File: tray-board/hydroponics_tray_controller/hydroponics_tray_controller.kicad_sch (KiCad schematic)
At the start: 29 parts, among them J1 Jumper, J2 Display_Connector, J4 Power_Comms, J5 i2c_Peripherals, J6 1Wire_Peripherals, SW1 RotaryEncoder_Switch, U1 ESP32, U2 SP3485EN, U3 AMS1117-3.3

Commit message: tray-board: replace ST7789 display connector with ILI9341 touch + SD card
J2 is now a 14-pin header matching the actual ILI9341/XPT2046 touch
display (VCC, GND, CS, RESET, DC, MOSI, SCK, LED, MISO, T_CLK, T_CS,
T_DIN, T_DO, T_IRQ), replacing the old 8-pin no-touch ST7789 wiring.
Added J3, a separate 4-pin SD card connector sharing the display SPI
bus with its own CS line. New signals use previously-unused ESP32
GPIOs 14, 19, 34, 35. Verified via KiCad 10 ERC and netlist export.

PCB footprints synced from the updated schematic (Update PCB from
Schematic) - placement and routing for the new pins still needed.

README updated with the corrected display spec and pin list.

Co-Authored-By: Claude Sonnet 5 <noreply@anthropic.com>
Claude-Session: https://claude.ai/code/session_01QYbZEgBzGJ6rSai1ie8nG1
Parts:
- added J3: SD_Connector, Connector_PinHeader_2.54mm:PinHeader_1x04_P2.54mm_Vertical, symbol Connector:Conn_01x04_Socket
- J2: value Display_Connector -> Display_Connector_Touch; footprint Connector_PinHeader_2.54mm:PinHeader_1x08_P2.54mm_Vertical -> Connector_PinHeader_2.54mm:PinHeader_1x14_P2.54mm_Vertical; symbol Connector:Conn_01x08_Socket -> Connector:Conn_01x14_Socket
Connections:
- net +3V3: now also J2.1 (Pin_1); no longer J2.2 (Pin_2)
- net ESP32_D18: now also J2.10 (Pin_10), J2.7 (Pin_7), J3.4 (Pin_4); no longer J2.3 (Pin_3)
- net ESP32_D2: now also J2.5 (Pin_5); no longer J2.6 (Pin_6)
- net ESP32_D23: now also J2.12 (Pin_12), J2.6 (Pin_6), J3.2 (Pin_2); no longer J2.4 (Pin_4)
- net ESP32_D4: now also J2.4 (Pin_4); no longer J2.5 (Pin_5)
- net ESP32_D5: now also J2.3 (Pin_3); no longer J2.7 (Pin_7)
- net GND: now also J2.2 (Pin_2); no longer J2.1 (Pin_1)
- net ESP32_D14: now reaches U1.10 (D14)
- net ESP32_D14: now also J2.11 (Pin_11)
- net ESP32_D19: now reaches U1.19 (D19)
- net ESP32_D19: now also J3.1 (Pin_1)
- net ESP32_D35: now reaches U1.22 (D35)
- net ESP32_D35: now also J2.14 (Pin_14)
- net ESP32_D34: now reaches U1.24 (D34)
- net ESP32_D34: now also J2.13 (Pin_13), J2.9 (Pin_9), J3.3 (Pin_3)
- no-connect marks 11 -> 7
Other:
- note added: "SD Card Connector"

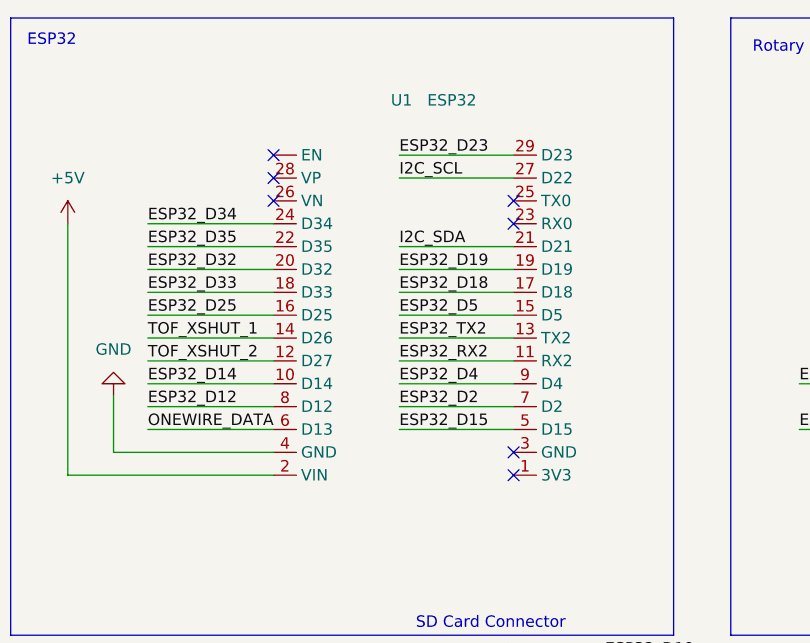
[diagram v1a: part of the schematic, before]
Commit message: JLCPCB prep: fab.sh cleanup, DNP the ESP32 module, BOM part-value fixes
tools/fab.sh:
- Gerbers use Protel extensions (JLCPCB's preferred naming) instead of
  --no-protel-ext.
- Drill export splits PTH/NPTH into separate Excellon files
  (--excellon-separate-th) instead of one merged file.
- BOM export now pulls the LCSC field (matching what's actually used in
  the schematics) instead of a nonexistent MPN field, groups by
  Value+Footprint+LCSC so parts sharing a value but not an LCSC code
  don't get merged together and silently lose their code, and excludes
  DNP parts.
- Pick-and-place (now named *-cpl.csv) already excluded DNP/THT; BOM
  now matches.
- Final zip only includes the gerbers + drill files JLCPCB needs, not
  the .gbrjob/drill-map files kicad-cli also generates.
- ERC gate relaxed to error-only: a stale lib_symbol_mismatch warning
  on the ESP32 symbol (harmless - doesn't affect connectivity or fab
  output) was blocking the pipeline; DRC stays error+warning.

Mark the socketed ESP32 DevKit (U1) Do-Not-Populate in both boards'
schematics, since it's a module the user fits themselves rather than
something JLCPCB should source/place - this drops it from BOM and CPL
automatically.

Fix a stale pin-number mismatch in reservoir-board's New_Library.kicad_sym
(ESP32 EN pin was "" in the library file but "30" in the schematic's
cached copy) that was one cause of the ERC warning above.

Also includes reservoir-board BOM part-value corrections (D_Schottky ->
SS34, bare resistor values -> "<value> Ohm") made directly in KiCad.

Co-Authored-By: Claude Sonnet 5 <noreply@anthropic.com>
Claude-Session: https://claude.ai/code/session_01QYbZEgBzGJ6rSai1ie8nG1
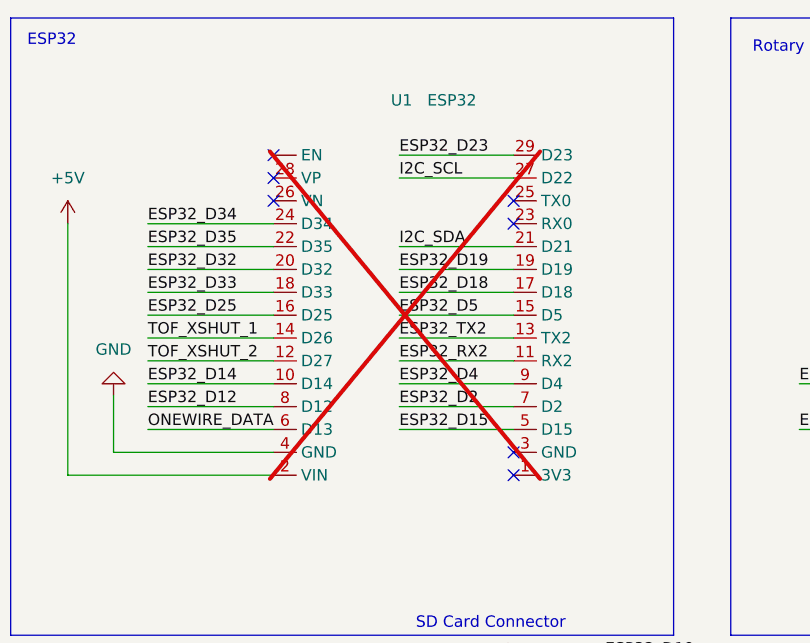
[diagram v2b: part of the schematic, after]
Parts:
- U1: now not fitted
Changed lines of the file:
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@@
 		(on_board yes)
 		(in_pos_files yes)
-		(dnp no)
+		(dnp yes)
 		(property "Reference" "U1"
 			(at 165.354 28.194 0)

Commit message: tray-board: fix EN pin number drift and J3 pin4 dangling wire
Same New_Library.kicad_sym drift as reservoir-board (EN pin number ""
in the library file vs "30" in the schematic's cached copy, matching
the ESP32_DevKit_30Pin footprint's pad "30") - tray-board's copy had
the same stale "" left over, just never triggered ERC since nothing
here referenced pin 30 by name at the time it was last checked.

J3 (SD connector) pin 4's wire started 1.27mm short of the actual pin
position - a leftover construction slip from when J3 was first added,
surfaced now as a real ERC error after the pin got moved during the
in-progress redesign. Fixed to reach the pin.

Co-Authored-By: Claude Sonnet 5 <noreply@anthropic.com>
Claude-Session: https://claude.ai/code/session_01QYbZEgBzGJ6rSai1ie8nG1
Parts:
- removed C6, C7: 100nF, Capacitor_SMD:C_0805_2012Metric, symbol Device:C
- removed R6, R7, R8: 10k, Resistor_SMD:R_0805_2012Metric, symbol Device:R
- removed SW1: RotaryEncoder_Switch, Rotary_Encoder:RotaryEncoder_Alps_EC11E-Switch_Vertical_H20mm, symbol Device:RotaryEncoder_Switch
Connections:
- net RS485_A: now also J4.3 (Pin_3); no longer J4.2 (Pin_2)
- net RS485_B: now also J4.2 (Pin_2); no longer J4.3 (Pin_3)
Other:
- note removed: "Rotary Encoder"
- moved on the sheet: J3

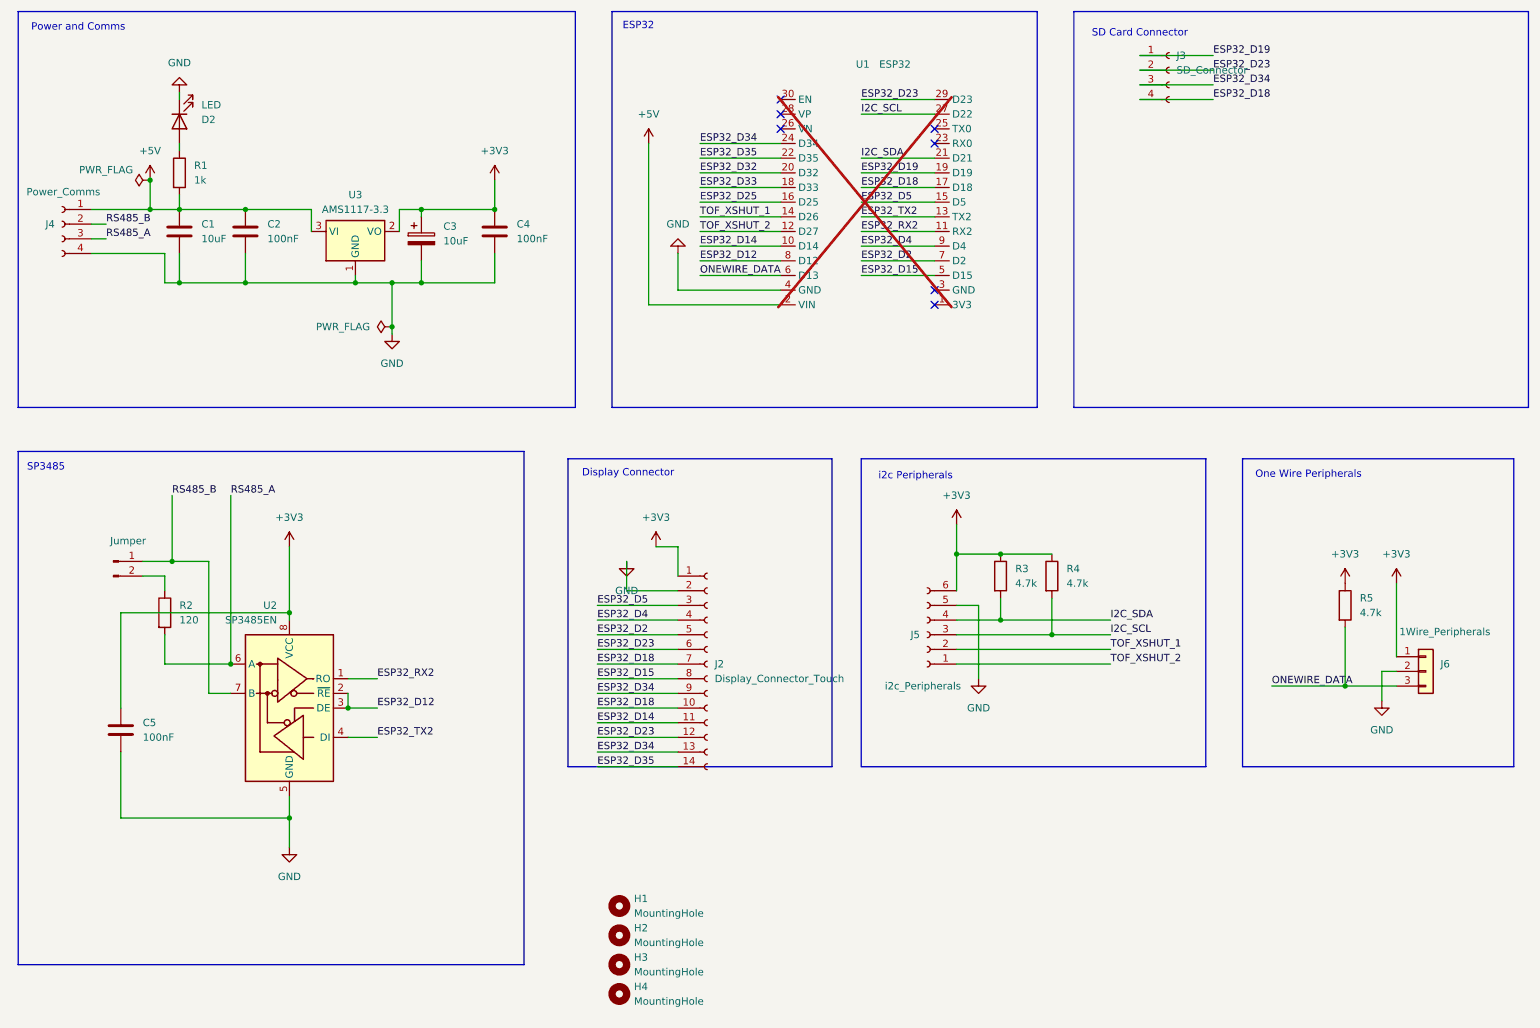
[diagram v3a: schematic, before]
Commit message: tray-board: merge display+SD connector into one symbol, fix SD pad position, re-sync PCB
- New_Library: merged the 14-pin main header and 4-pin SD header into a
  single Display_MSP2401_2.4in_Touch schematic symbol, matching the combined
  footprint's fixed connector spacing. J3 (standalone SD connector) removed;
  its nets are now carried by the merged symbol's SD1-SD4 pins.
- Footprint: fixed SD1-SD4 pad Y-coordinate (6.51mm -> 3.00mm from the top
  edge) - they sit in the same row as the two top mounting holes, per the
  mechanical drawing.
- Fixed H1-H4 mounting hole footprint (MountingHole_3.2mm_M3_Pad_Via ->
  MountingHole_3.2mm_M3) to match their "no connection" schematic symbol.
- kicad_pcb re-synced from schematic (Update PCB from Schematic + footprint
  reload) - layout/routing still in progress.

Co-Authored-By: Claude Sonnet 5 <noreply@anthropic.com>
Claude-Session: https://claude.ai/code/session_01QYbZEgBzGJ6rSai1ie8nG1
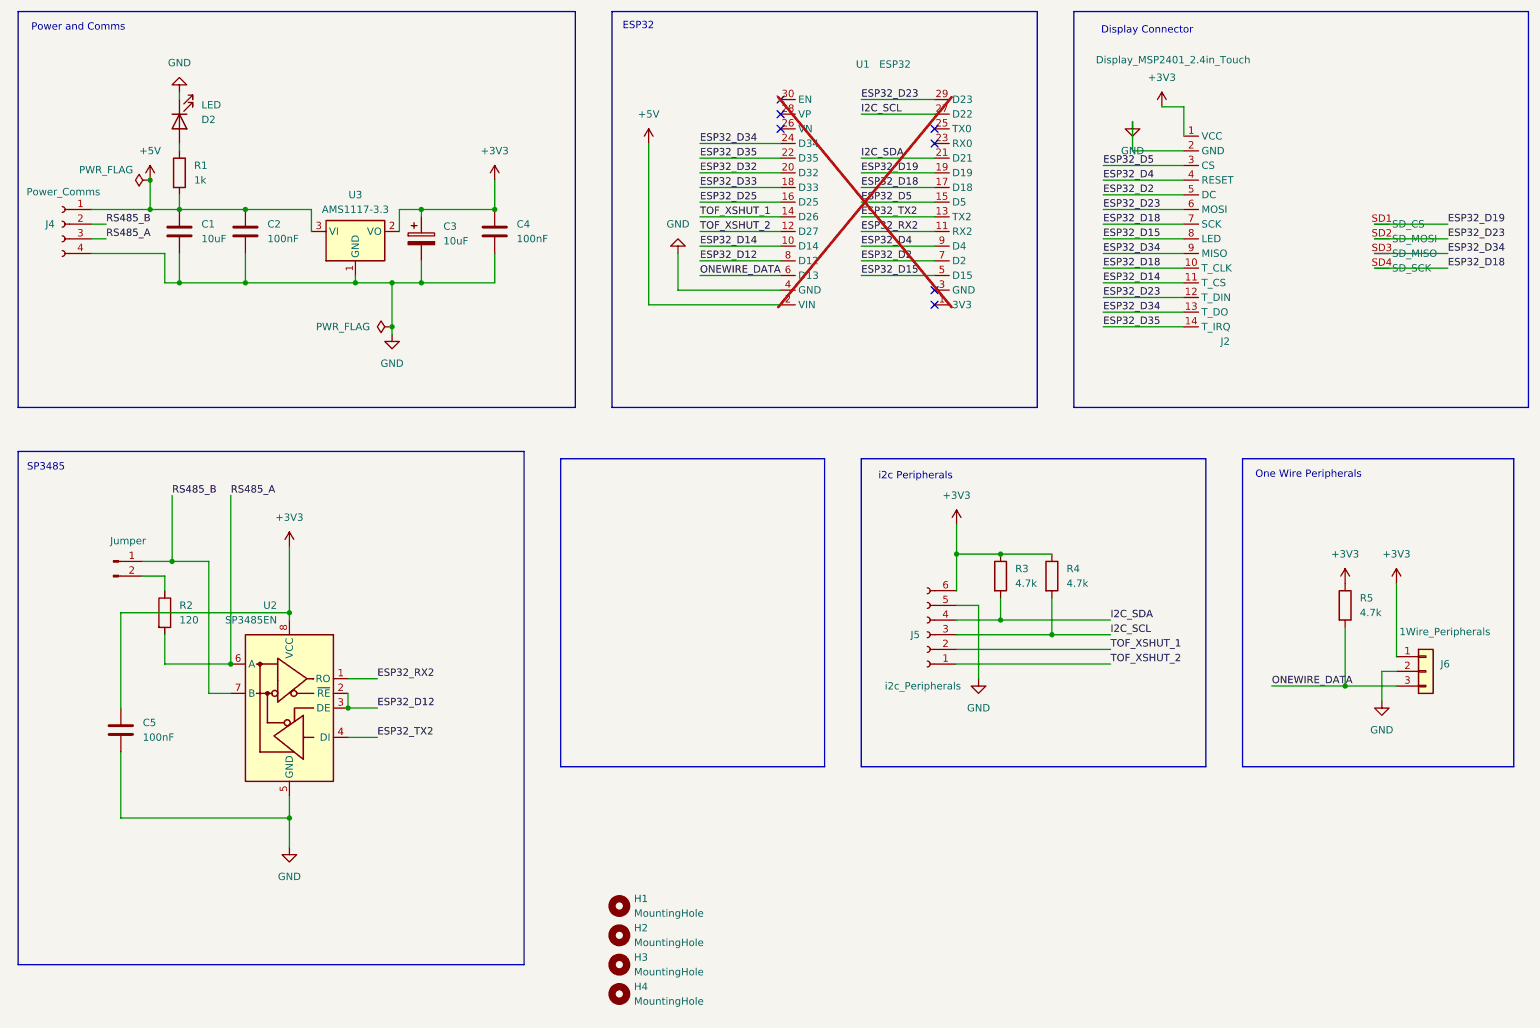
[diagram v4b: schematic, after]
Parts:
- removed J3: SD_Connector, Connector_PinHeader_2.54mm:PinHeader_1x04_P2.54mm_Vertical, symbol Connector:Conn_01x04_Socket
- H1, H2, H3, H4: footprint MountingHole:MountingHole_3.2mm_M3_Pad_Via -> MountingHole:MountingHole_3.2mm_M3
- J2: value Display_Connector_Touch -> Display_MSP2401_2.4in_Touch; footprint Connector_PinHeader_2.54mm:PinHeader_1x14_P2.54mm_Vertical -> Library:Display_MSP2401_2.4in_Touch; symbol Connector:Conn_01x14_Socket -> New_Library:Display_MSP2401_2.4in_Touch
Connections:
- net ESP32_D18: now also J2.SD4 (SD_SCK)
- net ESP32_D19: now also J2.SD1 (SD_CS)
- net ESP32_D23: now also J2.SD2 (SD_MOSI)
- net ESP32_D34: now also J2.SD3 (SD_MISO)
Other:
- note removed: "SD Card Connector"

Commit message: tray-board: ground plane fix, stitching, C3 ceramic swap, full JLC BOM
- F.Cu ground zone was netless with island-removal off, filling as ~26
  isolated islands (DRC isolated_copper). Assigned to GND, islands removed.
- Added ~18 GND stitching vias (ICs, decoupling caps, ESP32 centreline).
- Mounting holes H1-H4 swapped to MountingHole_Pad symbols wired to GND;
  the _Pad_Via footprints now bond both pours at all four corners.
- C3 changed from 10uF tantalum (EIA-3528-21, JLC Extended) to 10uF 25V
  X5R 0805 ceramic (C15850, Basic) - board is now Basic-only.
- Populated LCSC part numbers for all 13 SMD parts, stock/Basic-checked.
- Restored the board silkscreen title dropped in the earlier re-sync.
- kicad_pro: zone default min_clearance.

ERC / DRC / schematic-parity all clean.

Co-Authored-By: Claude Sonnet 5 <noreply@anthropic.com>
Claude-Session: https://claude.ai/code/session_01AfKCQW2p52QuPuRZiddque
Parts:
- C1: LCSC (none) -> C13585
- C2, C4, C5: LCSC (none) -> C49678
- C3: footprint Capacitor_Tantalum_SMD:CP_EIA-3528-21_Kemet-B -> Capacitor_SMD:C_0805_2012Metric; LCSC (none) -> C15850
- D2: LCSC (none) -> C2297
- H1, H2, H3, H4: footprint MountingHole:MountingHole_3.2mm_M3 -> MountingHole:MountingHole_3.2mm_M3_Pad_Via; symbol Mechanical:MountingHole -> Mechanical:MountingHole_Pad
- R1: LCSC (none) -> C17513
- R2: LCSC (none) -> C17437
- R3, R4, R5: LCSC (none) -> C17673
- U2: LCSC (none) -> C8963
- U3: LCSC (none) -> C6186
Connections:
- net GND: now also H1.1, H2.1, H3.1, H4.1
